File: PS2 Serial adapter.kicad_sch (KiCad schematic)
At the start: 11 parts, among them J1 PS2, J2 PC, U1 MAX3323EEUE

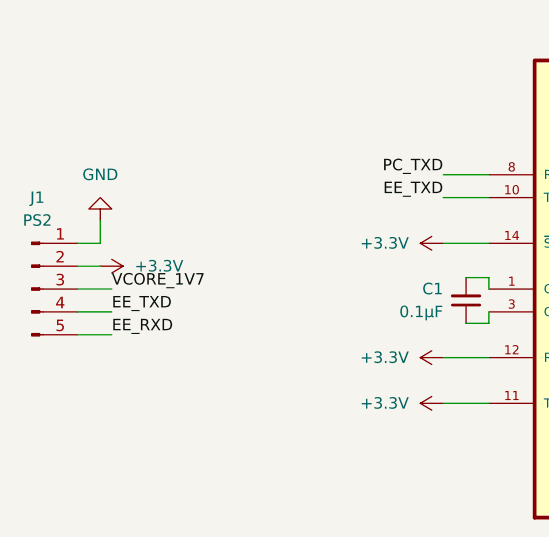
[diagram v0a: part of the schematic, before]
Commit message: Update footprints, 3V3 width and begin bom
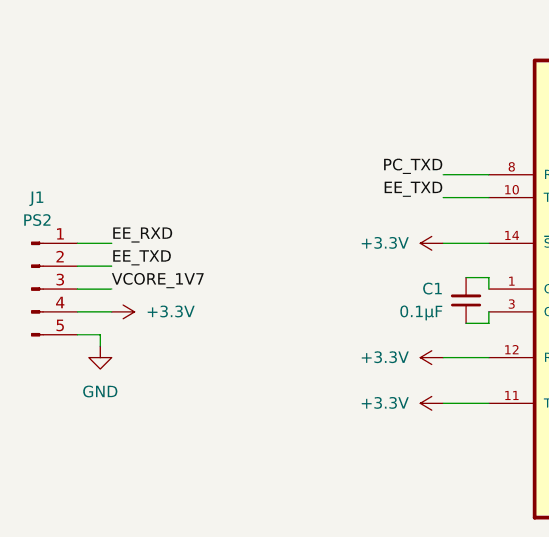
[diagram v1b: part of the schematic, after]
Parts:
- J1: footprint Connector_JST:JST_EH_S5B-EH_1x05_P2.50mm_Horizontal -> Connector_JST:JST_XH_S5B-XH-A_1x05_P2.50mm_Horizontal
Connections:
- net +3.3V: now also J1.4 (VCC_3V3); no longer J1.2 (VCC_3V3)
- net EE_RXD: now also J1.1 (EE_RXD); no longer J1.5 (EE_RXD)
- net EE_TXD: now also J1.2 (EE_TXD); no longer J1.4 (EE_TXD)
- net GND: now also J1.5 (GND); no longer J1.1 (GND)
